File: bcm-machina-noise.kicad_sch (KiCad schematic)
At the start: 64 parts, among them J1 USB_A, J2 AVR-ISP-6, Q1 2N5457, Q2 2N5457, SW1 SW_Push, U1 4069, U2 MCP602

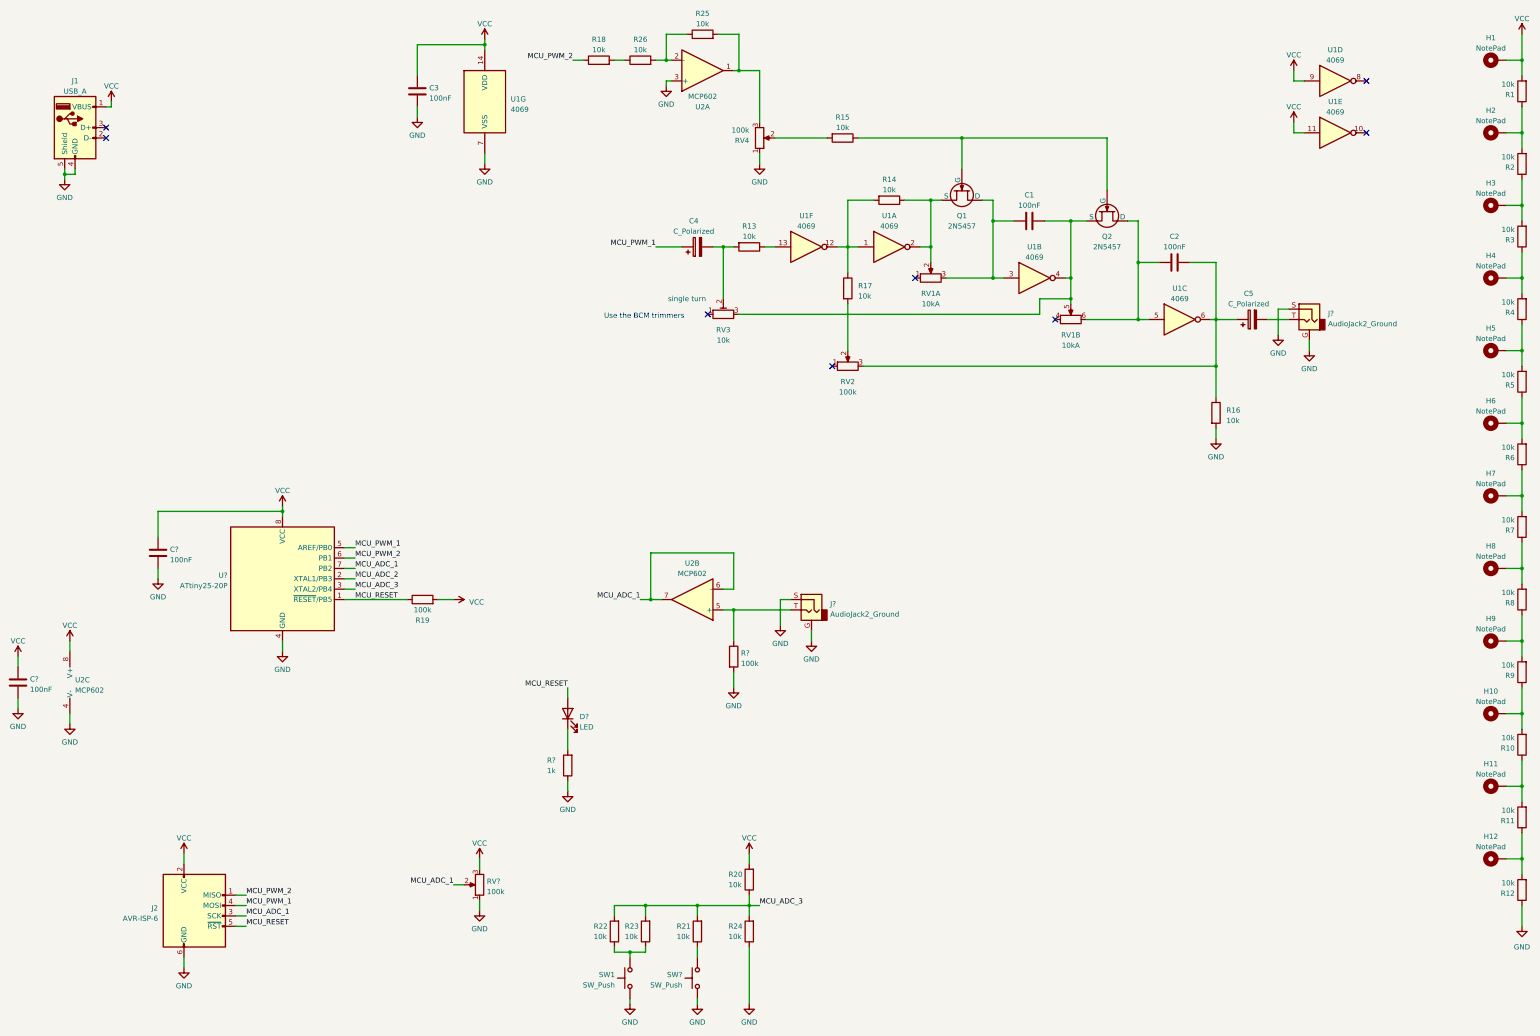
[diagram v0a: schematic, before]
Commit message: Attiny Chip Change
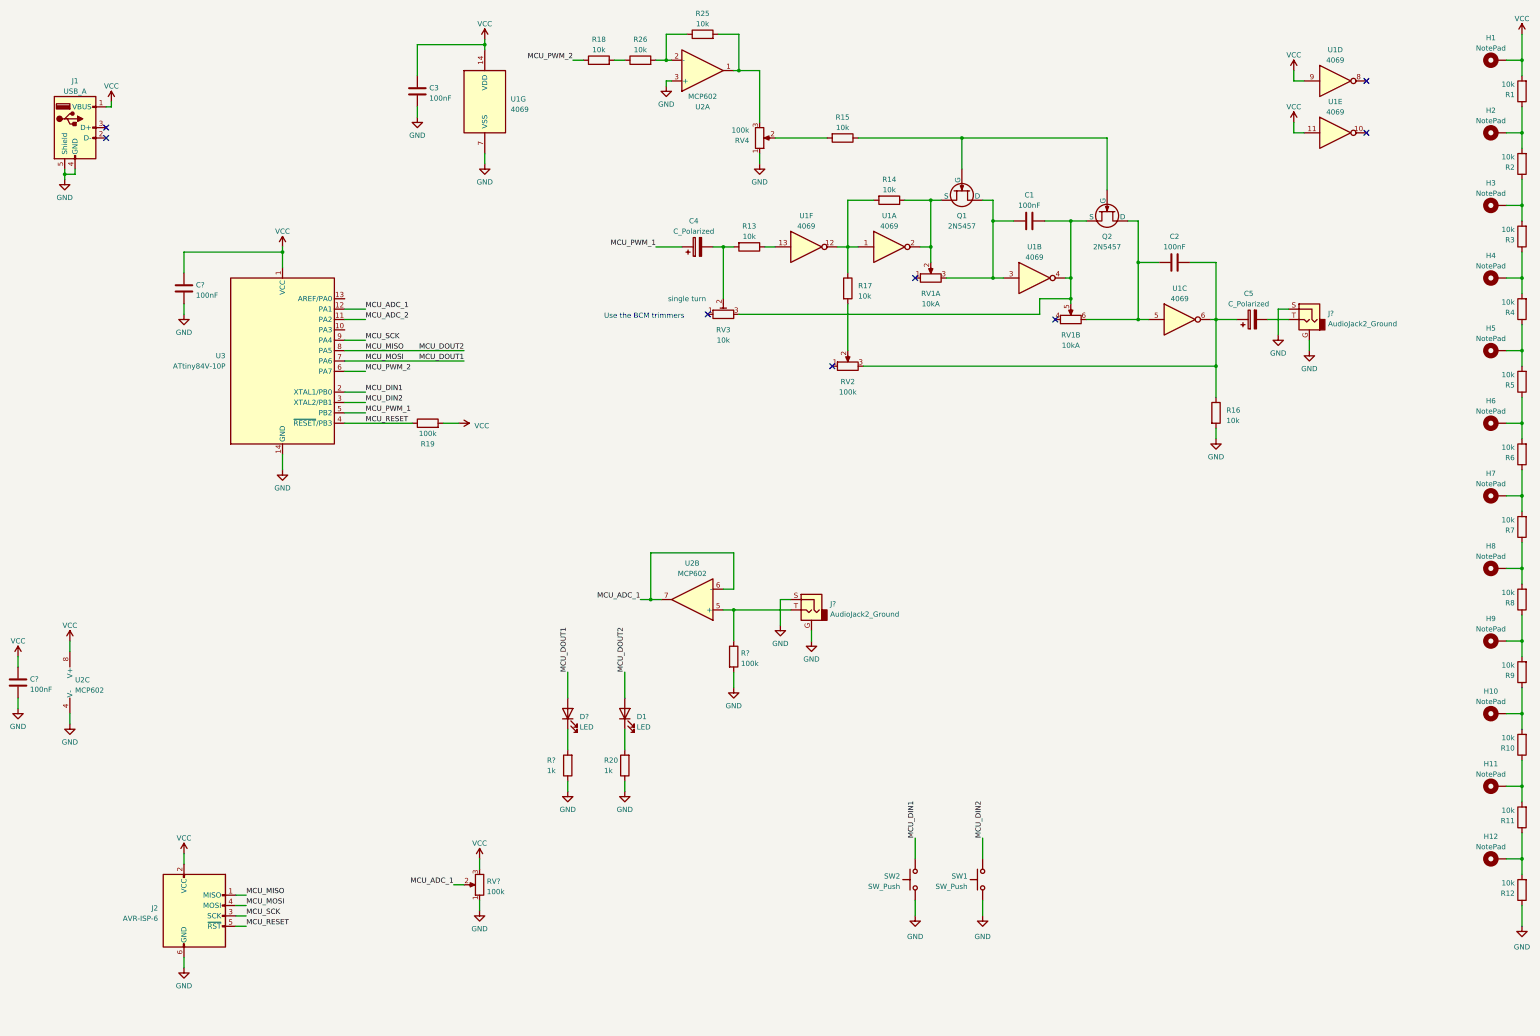
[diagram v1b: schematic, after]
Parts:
- removed R21, R22, R23, R24: 10k, rumblesan-standard-parts:R_Axial_DIN0207_L6.3mm_D2.5mm_P10.16mm_Horizontal, symbol rumblesan-standard-parts:R
- removed SW?: SW_Push, symbol Switch:SW_Push
- removed U?: ATtiny25-20P, Package_DIP:DIP-8_W7.62mm, symbol MCU_Microchip_ATtiny:ATtiny25-20P
- added D1: LED, symbol Device:LED
- added SW2: SW_Push, symbol Switch:SW_Push
- added U3: ATtiny84V-10P, Package_DIP:DIP-14_W7.62mm, symbol MCU_Microchip_ATtiny:ATtiny84V-10P
- R20: value 10k -> 1k
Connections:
- net MCU_ADC_3 is gone; now on net GND: R20.1
- net GND: now also SW2.2, U3.14 (GND)
- net MCU_ADC_1: now also U3.12 (PA1); no longer J2.3 (SCK)
- net MCU_ADC_2: now also U3.11 (PA2)
- net MCU_PWM_1: now also U3.5 (PB2); no longer J2.4 (MOSI)
- net MCU_PWM_2: now also U3.6 (PA7); no longer J2.1 (MISO)
- net MCU_RESET: now also U3.4 (~{RESET}/PB3); no longer D?.2 (A)
- net VCC: now also U3.1 (VCC); no longer R20.2
- net MCU_DIN2: now reaches SW1.1
- net MCU_DIN2: now also U3.3 (XTAL2/PB1)
- new net: D1.1 (K), R20.2
- new net MCU_DIN1: SW2.1, U3.2 (XTAL1/PB0)
- new net MCU_DOUT1: D?.2 (A), J2.4 (MOSI), U3.7 (PA6)
- new net MCU_DOUT2: D1.2 (A), J2.1 (MISO), U3.8 (PA5)
- new net MCU_SCK: J2.3 (SCK), U3.9 (PA4)
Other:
- moved on the sheet: C?, R19

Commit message: set schematic symbol to new USBpower footprint
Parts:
- C1, C2: footprint Rumblesan_Standard_Parts:C_Rect_L7.0mm_W3.5mm_P5.00mm -> Capacitor_THT:C_Rect_L7.0mm_W3.5mm_P5.00mm
- C3: footprint rumblesan-standard-parts:C_Rect_L7.0mm_W2.5mm_P5.00mm -> Capacitor_THT:C_Rect_L7.0mm_W3.5mm_P5.00mm
- C4, C5: footprint Rumblesan_Standard_Parts:C_Radial_D5.0mm_H5.0mm_P2.00mm -> Capacitor_THT:CP_Radial_D5.0mm_P2.00mm
- C6, C7: renamed from C?; footprint rumblesan-standard-parts:C_Rect_L7.0mm_W2.5mm_P5.00mm -> Capacitor_THT:C_Rect_L7.0mm_W3.5mm_P5.00mm
- D1: footprint (none) -> LED_THT:LED_D5.0mm
- D2: renamed from D?; footprint (none) -> LED_THT:LED_D5.0mm
- H1, H10, H11, H12, H2, H3, H4, H5, H6, H7, H8, H9: footprint (none) -> MountingHole:MountingHole_4.3mm_M4_DIN965_Pad
- J1: footprint (none) -> USBPower:AMPHENOL_10103593-0001LF
- J2, RV1: footprint (none) -> Connector_PinHeader_2.54mm:PinHeader_2x03_P2.54mm_Vertical
- J3, J4: renamed from J?; footprint (none) -> Connector_Audio:Jack_3.5mm_QingPu_WQP-PJ398SM_Vertical_CircularHoles
- Q1, Q2, U2: footprint (none) -> Package_TO_SOT_THT:TO-92L_Inline_Wide
- R1, R10, R11, R12, R13, R14, R15, R16, R17, R18, R2, R20, R25, R26, R3, R4, R5, R6, R7, R8, R9: footprint rumblesan-standard-parts:R_Axial_DIN0207_L6.3mm_D2.5mm_P10.16mm_Horizontal -> Resistor_THT:R_Axial_DIN0207_L6.3mm_D2.5mm_P10.16mm_Horizontal
- R19: footprint Rumblesan_Standard_Parts:R_Axial_DIN0207_L6.3mm_D2.5mm_P10.16mm_Horizontal -> Resistor_THT:R_Axial_DIN0207_L6.3mm_D2.5mm_P10.16mm_Horizontal
- R21, R22: renamed from R?; footprint rumblesan-standard-parts:R_Axial_DIN0207_L6.3mm_D2.5mm_P10.16mm_Horizontal -> Resistor_THT:R_Axial_DIN0207_L6.3mm_D2.5mm_P10.16mm_Horizontal
- RV2, RV4: footprint Rumblesan_Standard_Parts:Potentiometer_Alpha_RD901F-40-00D_Single_Vertical -> Potentiometer_THT:Potentiometer_Alpha_RD901F-40-00D_Single_Vertical
- RV3: footprint Rumblesan_Standard_Parts:Potentiometer_THT_Bourns_3306P_Vertical -> Potentiometer_THT:Potentiometer_Alpha_RD902F-40-00D_Dual_Vertical
- RV5: renamed from RV?; footprint (none) -> Potentiometer_THT:Potentiometer_Alpha_RD902F-40-00D_Dual_Vertical
- SW1, SW2: footprint (none) -> Button_Switch_THT:SW_PUSH_6mm
- U1: footprint (none) -> Package_DIP:DIP-14_W7.62mm

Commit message: fixed errors
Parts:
- C1, C2: symbol Rumblesan Standard Parts:C -> Device:C
- C3, C6, C7: symbol rumblesan-standard-parts:C -> Device:C
- C4, C5: symbol Rumblesan Standard Parts:C_Polarized -> Device:C_Polarized
- J3, J4: symbol Connector:AudioJack2_Ground -> Connector_Audio:AudioJack2_Ground
- R1, R10, R11, R12, R2, R20, R21, R22, R3, R4, R5, R6, R7, R8, R9: symbol rumblesan-standard-parts:R -> Device:R
- R13, R14, R15, R16, R17, R18, R19, R25, R26: symbol Rumblesan Standard Parts:R -> Device:R
- RV2, RV4: symbol Rumblesan Standard Parts:R_Potentiometer -> Device:R_Potentiometer
- RV3: symbol Rumblesan Standard Parts:R_Potentiometer_Trim -> Device:R_Potentiometer_Trim
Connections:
- net GND: now also R12.2, R16.1, R20.2, R21.2, R22.1; no longer R12.1, R16.2, R20.1, R21.1, R22.2
- net MCU_ADC_1: no longer RV5.2
- net MCU_ADC_2: now also RV5.2
- net MCU_PWM_2: now also R18.2; no longer R18.1
- net MCU_RESET: now also R19.2; no longer R19.1
- net VCC: now also R1.1, R19.1; no longer R1.2, R19.2
- net at U1.1, U1.12: now also R14.1, R17.2; no longer R14.2, R17.1
- net at Q1.3 (S), RV1.2, U1.2: now also R14.2; no longer R14.1
- net at C2.2, C5.1, RV2.3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: now also R16.2; no longer R16.1
- net at C4.2, RV3.2: now also R13.1; no longer R13.2
- net at U1.13: now also R13.2; no longer R13.1
- net at D2.1 (K): now also R21.1; no longer R21.2
- net at RV4.3, U2.1: now also R25.1; no longer R25.2
- net at R26.1: now also R25.2, U2.2 (-); no longer R18.2
- net at Q1.2 (G), Q2.2 (G): now also R15.2; no longer R15.1
- net at RV4.2: now also R15.1; no longer R15.2
- net at J3.T, U2.5 (+): now also R22.2; no longer R22.1
- net at RV2.2: now also R17.1; no longer R17.2
- net at D1.1 (K): now also R20.1; no longer R20.2
- new net: H11.1, R10.2, R11.1
- new net: H12.1, R11.2, R12.1
- new net: H4.1, R3.2, R4.1
- new net: H8.1, R7.2, R8.1
- new net: H9.1, R8.2, R9.1
- new net: H5.1, R4.2, R5.1
- new net: H6.1, R5.2, R6.1
- new net: H2.1, R1.2, R2.1
- new net: H3.1, R2.2, R3.1
- new net: H7.1, R6.2, R7.1
- new net: H10.1, R10.1, R9.2
- new net: R18.1, R26.2
- no-connect marks 8 -> 10

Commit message: more bug fixes
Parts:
- removed J3, J4: AudioJack2_Ground, Connector_Audio:Jack_3.5mm_QingPu_WQP-PJ398SM_Vertical_CircularHoles, symbol Connector_Audio:AudioJack2_Ground
- added J3, J5: AudioJack2_SwitchT, Connector_Audio:Jack_3.5mm_QingPu_WQP-PJ398SM_Vertical_CircularHoles, symbol Connector_Audio:AudioJack2_SwitchT
- RV1: footprint Connector_PinHeader_2.54mm:PinHeader_2x03_P2.54mm_Vertical -> Potentiometer_THT:Potentiometer_Alpha_RD902F-40-00D_Dual_Vertical
- U2: footprint Package_TO_SOT_THT:TO-92L_Inline_Wide -> Package_DIP:DIP-8_W7.62mm
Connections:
- net GND: now also J3.S, J5.S
- net at C5.2: now also J3.T
- net at R22.2, U2.5 (+): now also J5.T
- no-connect marks 10 -> 12
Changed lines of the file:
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@@
   (no_connect (at 104.14 88.9))
   (no_connect (at 45.72 49.53))
+  (no_connect (at 213.36 167.64))
   (no_connect (at 278.13 93.98))
   (no_connect (at 243.84 83.82))
+  (no_connect (at 335.28 96.52))
   (no_connect (at 354.33 35.56))
   (no_connect (at 45.72 46.99))
@@
     (stroke (width 0) (type default))
   )
-  (wire (pts (xy 340.36 99.06) (xy 340.36 101.6))
-    (stroke (width 0) (type default))
-  )
   (wire (pts (xy 77.47 242.57) (xy 80.01 242.57))
     (stroke (width 0) (type default))
@@
     (stroke (width 0) (type default))
   )
-  (wire (pts (xy 218.44 170.18) (xy 218.44 172.72))
-    (stroke (width 0) (type default))
-  )
   (wire (pts (xy 317.5 120.65) (xy 317.5 123.19))
     (stroke (width 0) (type default))
@@
     )
   )
-  (symbol (lib_id "Connector_Audio:AudioJack2_Ground") (at 340.36 93.98 0) (mirror y) (unit 1)
-    (in_bom yes) (on_board yes) (dnp no) (fields_autoplaced)
-    (property "Reference" "J4" (at 344.932 92.5103 0)
-      (effects (font (size 1.27 1.27)) (justify right))
-    )
-    (property "Value" "AudioJack2_Ground" (at 344.932 95.0472 0)
-      (effects (font (size 1.27 1.27)) (justify right))
-    )
-    (property "Footprint" "Connector_Audio:Jack_3.5mm_QingPu_WQP-PJ398SM_Vertical_CircularHoles" (at 340.36 93.98 0)
-      (effects (font (size 1.27 1.27)) hide)
-    )
-    (property "Datasheet" "~" (at 340.36 93.98 0)
-      (effects (font (size 1.27 1.27)) hide)
-    )
-    (pin "G")
-    (pin "S")
-    (pin "T")
-    (instances
-      (project "bcm-machina-noise"
-        (path "/5b0acaca-dc50-4fa5-b146-164c1b9ad031"
-          (reference "J4") (unit 1)
-        )
-      )
-    )
-  )
   (symbol (lib_id "power:PWR_FLAG") (at 57.15 39.37 0) (unit 1)
     (in_bom yes) (on_board yes) (dnp no) (fields_autoplaced)
@@
     )
   )
+  (symbol (lib_id "Connector_Audio:AudioJack2_SwitchT") (at 218.44 165.1 0) (mirror y) (unit 1)
+    (in_bom yes) (on_board yes) (dnp no)
+    (property "Reference" "J5" (at 219.075 156.21 0)
+      (effects (font (size 1.27 1.27)))
+    )
+    (property "Value" "AudioJack2_SwitchT" (at 219.075 158.75 0)
+      (effects (font (size 1.27 1.27)))
+    )
+    (property "Footprint" "Connector_Audio:Jack_3.5mm_QingPu_WQP-PJ398SM_Vertical_CircularHoles" (at 218.44 165.1 0)
+      (effects (font (size 1.27 1.27)) hide)
+    )
+    (property "Datasheet" "~" (at 218.44 165.1 0)
+      (effects (font (size 1.27 1.27)) hide)
+    )
+    (pin "S")
+    (pin "T")
+    (pin "TN")
+    (instances
+      (project "bcm-machina-noise"
+        (path "/5b0acaca-dc50-4fa5-b146-164c1b9ad031"
+          (reference "J5") (unit 1)
+        )
+      )
+    )
+  )
   (symbol (lib_id "Device:R_Potentiometer_Dual_Separate") (at 281.94 93.98 90) (unit 2)
     (in_bom yes) (on_board yes) (dnp no) (fields_autoplaced)
@@
       (effects (font (size 1.27 1.27)))
     )
-    (property "Footprint" "Connector_PinHeader_2.54mm:PinHeader_2x03_P2.54mm_Vertical" (at 281.94 93.98 0)
+    (property "Footprint" "Potentiometer_THT:Potentiometer_Alpha_RD902F-40-00D_Dual_Vertical" (at 281.94 93.98 0)
       (effects (font (size 1.27 1.27)) hide)
     )
@@
     )
   )
+  (symbol (lib_id "Connector_Audio:AudioJack2_SwitchT") (at 340.36 93.98 0) (mirror y) (unit 1)
+    (in_bom yes) (on_board yes) (dnp no)
+    (property "Reference" "J3" (at 340.995 85.09 0)
+      (effects (font (size 1.27 1.27)))
+    )
+    (property "Value" "AudioJack2_SwitchT" (at 340.995 87.63 0)
+      (effects (font (size 1.27 1.27)))
+    )
+    (property "Footprint" "Connector_Audio:Jack_3.5mm_QingPu_WQP-PJ398SM_Vertical_CircularHoles" (at 340.36 93.98 0)
+      (effects (font (size 1.27 1.27)) hide)
+    )
+    (property "Datasheet" "~" (at 340.36 93.98 0)
+      (effects (font (size 1.27 1.27)) hide)
+    )
+    (pin "S")
+    (pin "T")
+    (pin "TN")
+    (instances
+      (project "bcm-machina-noise"
+        (path "/5b0acaca-dc50-4fa5-b146-164c1b9ad031"
+          (reference "J3") (unit 1)
+        )
+      )
+    )
+  )
   (symbol (lib_id "power:VCC") (at 138.43 25.4 0) (unit 1)
     (in_bom yes) (on_board yes) (dnp no) (fields_autoplaced)
@@
     )
   )
-  (symbol (lib_id "Connector_Audio:AudioJack2_Ground") (at 218.44 165.1 0) (mirror y) (unit 1)
-    (in_bom yes) (on_board yes) (dnp no) (fields_autoplaced)
-    (property "Reference" "J3" (at 223.012 163.6303 0)
-      (effects (font (size 1.27 1.27)) (justify right))
-    )
-    (property "Value" "AudioJack2_Ground" (at 223.012 166.1672 0)
-      (effects (font (size 1.27 1.27)) (justify right))
-    )
-    (property "Footprint" "Connector_Audio:Jack_3.5mm_QingPu_WQP-PJ398SM_Vertical_CircularHoles" (at 218.44 165.1 0)
-      (effects (font (size 1.27 1.27)) hide)
-    )
-    (property "Datasheet" "~" (at 218.44 165.1 0)
-      (effects (font (size 1.27 1.27)) hide)
-    )
-    (pin "G")
-    (pin "S")
-    (pin "T")
-    (instances
-      (project "bcm-machina-noise"
-        (path "/5b0acaca-dc50-4fa5-b146-164c1b9ad031"
-          (reference "J3") (unit 1)
-        )
-      )
-    )
-  )
   (symbol (lib_id "Mechanical:MountingHole_Pad") (at 386.08 208.28 90) (unit 1)
     (in_bom yes) (on_board yes) (dnp no) (fields_autoplaced)
@@
       (effects (font (size 1.27 1.27)))
     )
-    (property "Footprint" "Package_TO_SOT_THT:TO-92L_Inline_Wide" (at 189.23 162.56 0)
+    (property "Footprint" "Package_DIP:DIP-8_W7.62mm" (at 189.23 162.56 0)
       (effects (font (size 1.27 1.27)) hide)
     )
@@
       (effects (font (size 1.27 1.27)))
     )
-    (property "Footprint" "Package_TO_SOT_THT:TO-92L_Inline_Wide" (at 191.77 33.02 0)
+    (property "Footprint" "Package_DIP:DIP-8_W7.62mm" (at 191.77 33.02 0)
       (effects (font (size 1.27 1.27)) hide)
     )
@@
     )
   )
-  (symbol (lib_id "power:GND") (at 340.36 101.6 0) (unit 1)
-    (in_bom yes) (on_board yes) (dnp no) (fields_autoplaced)
-    (property "Reference" "#PWR0109" (at 340.36 107.95 0)
-      (effects (font (size 1.27 1.27)) hide)
-    )
-    (property "Value" "GND" (at 340.36 106.0434 0)
-      (effects (font (size 1.27 1.27)))
-    )
-    (property "Footprint" "" (at 340.36 101.6 0)
-      (effects (font (size 1.27 1.27)) hide)
-    )
-    (property "Datasheet" "" (at 340.36 101.6 0)
-      (effects (font (size 1.27 1.27)) hide)
-    )
-    (pin "1")
-    (instances
-      (project "bcm-machina-noise"
-        (path "/5b0acaca-dc50-4fa5-b146-164c1b9ad031"
-          (reference "#PWR0109") (unit 1)
-        )
-      )
-    )
-  )
   (symbol (lib_id "Mechanical:MountingHole_Pad") (at 386.08 66.04 90) (unit 1)
     (in_bom yes) (on_board yes) (dnp no) (fields_autoplaced)
@@
       (effects (font (size 1.27 1.27)) (justify left))
     )
-    (property "Footprint" "Package_TO_SOT_THT:TO-92L_Inline_Wide" (at 39.37 182.88 0)
+    (property "Footprint" "Package_DIP:DIP-8_W7.62mm" (at 39.37 182.88 0)
       (effects (font (size 1.27 1.27)) hide)
     )
@@
     )
   )
-  (symbol (lib_id "power:GND") (at 218.44 172.72 0) (unit 1)
-    (in_bom yes) (on_board yes) (dnp no) (fields_autoplaced)
-    (property "Reference" "#PWR0111" (at 218.44 179.07 0)
-      (effects (font (size 1.27 1.27)) hide)
-    )
-    (property "Value" "GND" (at 218.44 177.1634 0)
-      (effects (font (size 1.27 1.27)))
-    )
-    (property "Footprint" "" (at 218.44 172.72 0)
-      (effects (font (size 1.27 1.27)) hide)
-    )
-    (property "Datasheet" "" (at 218.44 172.72 0)
-      (effects (font (size 1.27 1.27)) hide)
-    )
-    (pin "1")
-    (instances
-      (project "bcm-machina-noise"
-        (path "/5b0acaca-dc50-4fa5-b146-164c1b9ad031"
-          (reference "#PWR0111") (unit 1)
-        )
-      )
-    )
-  )
   (symbol (lib_id "Simulation_SPICE:NJFET") (at 255.27 62.23 270) (unit 1)
     (in_bom yes) (on_board yes) (dnp no) (fields_autoplaced)
@@
       (effects (font (size 1.27 1.27)))
     )
-    (property "Footprint" "Connector_PinHeader_2.54mm:PinHeader_2x03_P2.54mm_Vertical" (at 247.65 83.82 0)
+    (property "Footprint" "Potentiometer_THT:Potentiometer_Alpha_RD902F-40-00D_Dual_Vertical" (at 247.65 83.82 0)
       (effects (font (size 1.27 1.27)) hide)
     )

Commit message: starting layout
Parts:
- RV3: footprint Potentiometer_THT:Potentiometer_Alpha_RD902F-40-00D_Dual_Vertical -> Trimpot:Potentiometer_THT_Bourns_3306P_Vertical
- RV5: footprint Potentiometer_THT:Potentiometer_Alpha_RD902F-40-00D_Dual_Vertical -> Potentiometer_THT:Potentiometer_Alpha_RD901F-40-00D_Single_Vertical_CircularHoles
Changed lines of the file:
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@@
       (effects (font (size 1.27 1.27)) (justify right))
     )
-    (property "Footprint" "Potentiometer_THT:Potentiometer_Alpha_RD902F-40-00D_Dual_Vertical" (at 137.16 232.41 0)
+    (property "Footprint" "Potentiometer_THT:Potentiometer_Alpha_RD901F-40-00D_Single_Vertical_CircularHoles" (at 137.16 232.41 0)
       (effects (font (size 1.27 1.27)) hide)
     )
@@
       (effects (font (size 1.27 1.27)))
     )
-    (property "Footprint" "Potentiometer_THT:Potentiometer_Alpha_RD902F-40-00D_Dual_Vertical" (at 196.85 92.71 0)
-      (effects (font (size 1.27 1.27)) hide)
-    )
+    (property "Footprint" "Trimpot:Potentiometer_THT_Bourns_3306P_Vertical" (at 196.85 92.71 0)
+      (effects (font (size 1.27 1.27)) hide)
+    )
